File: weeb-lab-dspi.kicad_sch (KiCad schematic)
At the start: 11 parts, among them J1 SPDIF, J2 MONO RCA, U1 XIAO-RP2350-SMD

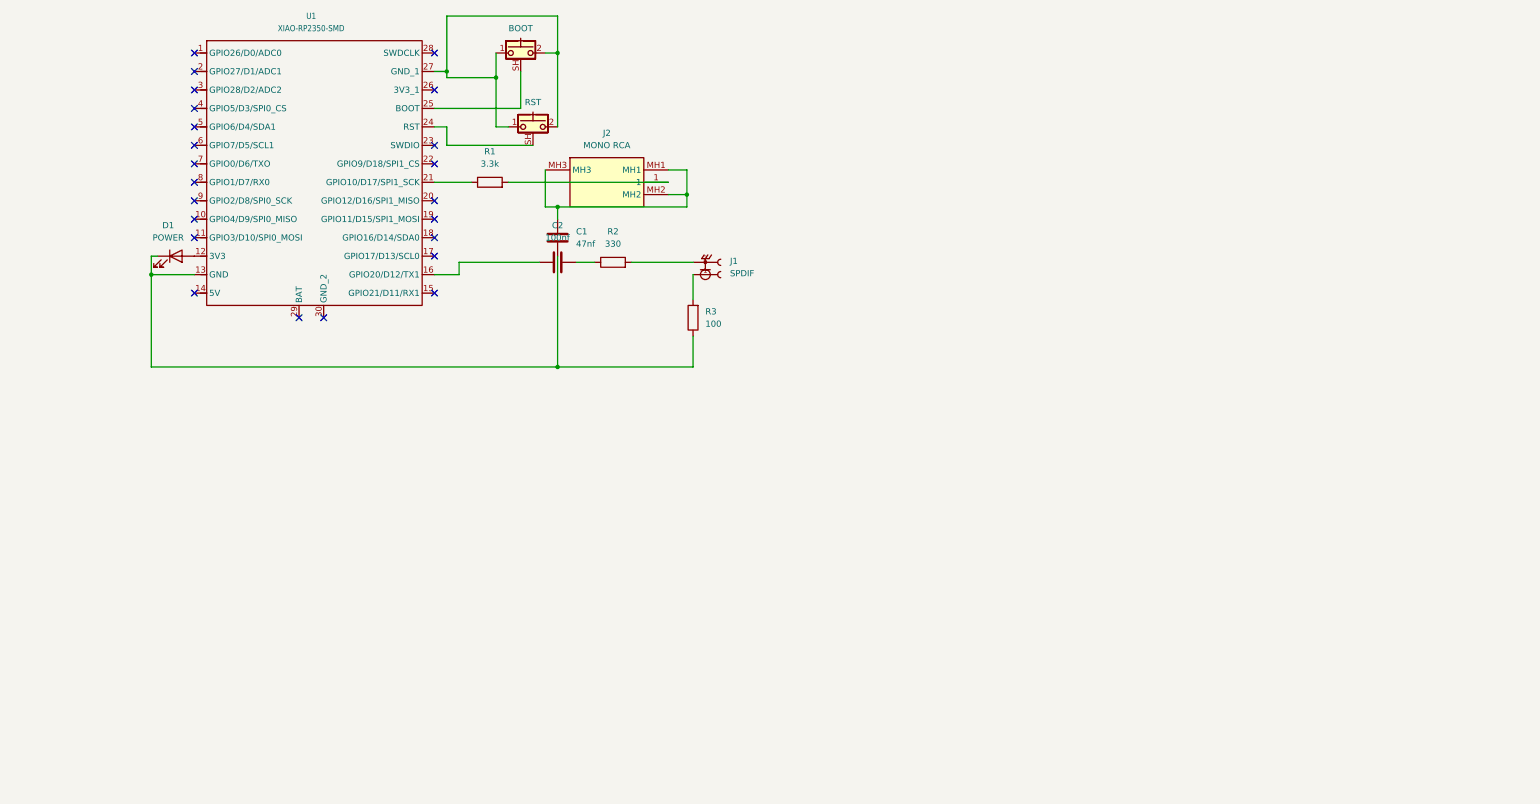
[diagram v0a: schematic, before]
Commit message: Routed PCB and added more parts
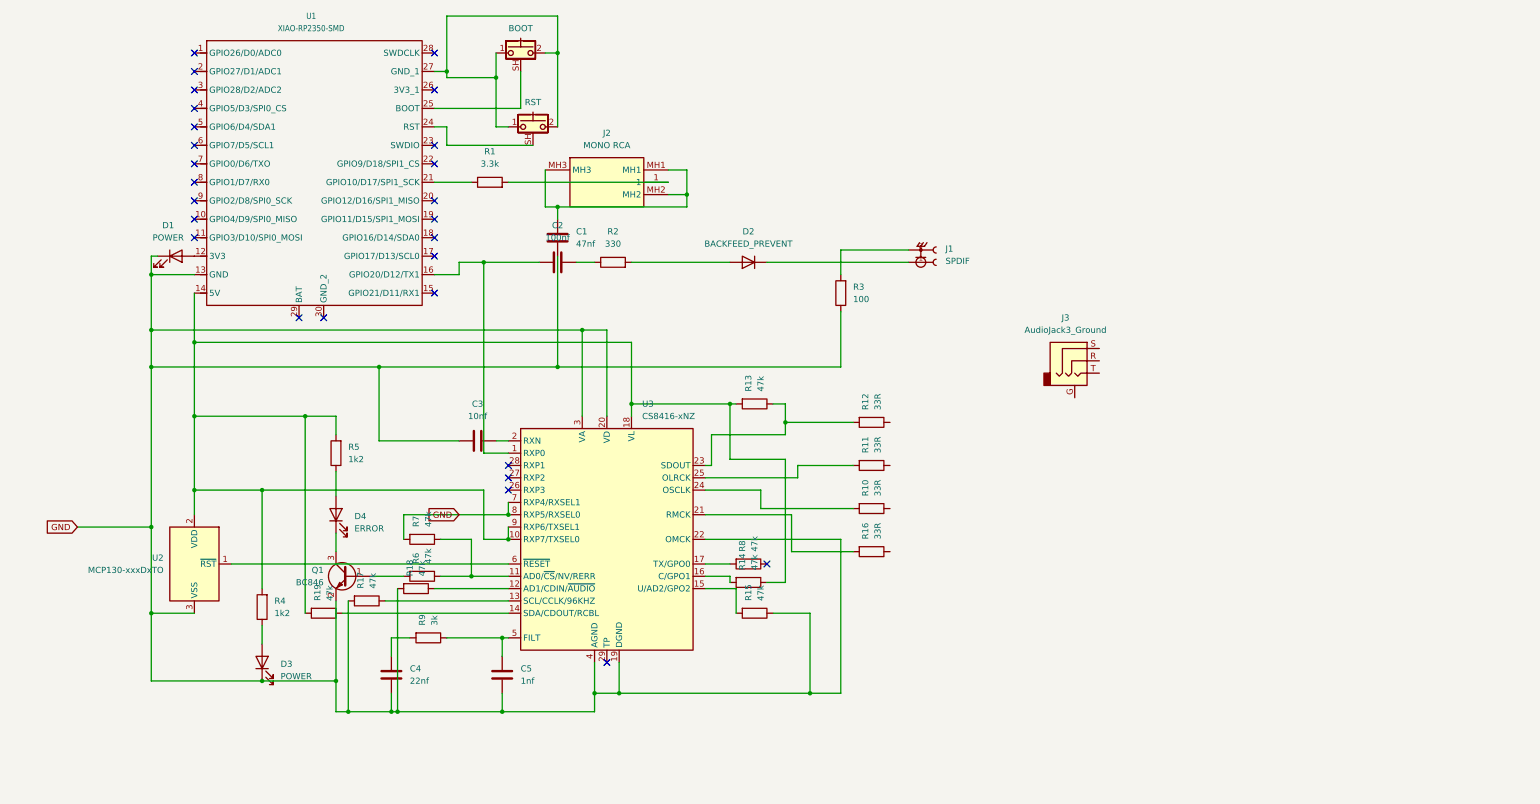
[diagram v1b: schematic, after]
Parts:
- added C3: 10nf, Capacitor_SMD:C_0402_1005Metric, symbol Device:C
- added C4: 22nf, Capacitor_SMD:C_0402_1005Metric, symbol Device:C
- added C5: 1nf, Capacitor_SMD:C_0402_1005Metric, symbol Device:C
- added D2: BACKFEED_PREVENT, Diode_SMD:D_0402_1005Metric, symbol Device:D
- added D3: POWER, LED_SMD:LED_0805_2012Metric, symbol Device:LED
- added D4: ERROR, LED_SMD:LED_0805_2012Metric, symbol Device:LED
- added J3: AudioJack3_Ground, Connector_Audio:Jack_3.5mm_KoreanHropartsElec_PJ-320D-4A_Horizontal, symbol Connector_Audio:AudioJack3_Ground
- added Q1: BC846, Package_TO_SOT_SMD:SOT-23-3, symbol Transistor_BJT:BC846
- added R10, R11, R12, R16: 33R, Resistor_SMD:R_0402_1005Metric, symbol Device:R
- added R13, R14, R15, R17, R18, R19, R6, R7, R8: 47k, Resistor_SMD:R_0402_1005Metric, symbol Device:R
- added R4, R5: 1k2, Resistor_SMD:R_0402_1005Metric, symbol Device:R
- added R9: 3k, Resistor_SMD:R_0402_1005Metric, symbol Device:R
- added U2: MCP130-xxxDxTO, Package_TO_SOT_THT:TO-92L_Inline_Wide, symbol Power_Supervisor:MCP130-xxxDxTO
- added U3: CS8416-xNZ, Package_SO:TSSOP-28_4.4x9.7mm_P0.65mm, symbol Audio:CS8416-xNZ
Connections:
- net GND: now reaches C1.2, D1.1 (K), R3.1, U1.13 (GND)
- net GND: now also C3.1, C4.2, C5.2, D3.1 (K), Q1.2 (E), R15.1, R17.2, R18.2, R7.2, U2.3 (VSS), U3.19 (DGND), U3.20 (VD), U3.22 (OMCK), U3.3 (VA), U3.4 (AGND), U3.7 (RXP4/RXSEL1), U3.8 (RXP5/RXSEL0)
- net at J1.2, J1.3, J1.4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: now also R3.2; no longer R2.2
- net at J1.1: now also D2.1 (K); no longer R3.2
- net at U1.14 (5V): now also R13.2, R14.1, R19.2, R4.2, R5.2, U2.2 (VDD), U3.10 (RXP7/TXSEL0), U3.18 (VL), U3.9 (RXP6/TXSEL1)
- net at C2.1, U1.16 (GPIO20/D12/TX1): now also U3.1 (RXP0)
- new net: R12.2, R13.1, U3.23 (SDOUT)
- new net: R17.1, U3.13 (SCL/CCLK/96KHZ)
- new net: D4.2 (A), R5.1
- new net: C4.1, R9.2
- new net: R10.2, U3.24 (OSCLK)
- new net: R11.2, U3.25 (OLRCK)
- new net: D2.2 (A), R2.2
- new net: R6.1, R7.1, U3.11 (AD0/~{CS}/NV/RERR)
- new net: R16.2, U3.21 (RMCK)
- new net: C3.2, U3.2 (RXN)
- new net: R14.2, U3.16 (C/GPO1)
- new net: Q1.1 (B), R6.2
- new net: U2.1 (~{RST}), U3.6 (~{RESET})
- new net: R19.1, U3.14 (SDA/CDOUT/RCBL)
- new net: R18.1, U3.12 (AD1/CDIN/~{AUDIO})
- new net: R15.2, U3.15 (U/AD2/GPO2)
- new net: R8.2, U3.17 (TX/GPO0)
- new net: C5.1, R9.1, U3.5 (FILT)
- new net: D4.1 (K), Q1.3 (C)
- new net: D3.2 (A), R4.1
- no-connect marks 23 -> 27
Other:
- moved on the sheet: J1, R3

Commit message: Almost  Complete
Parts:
- removed J3: AudioJack3_Ground, Connector_Audio:Jack_3.5mm_KoreanHropartsElec_PJ-320D-4A_Horizontal, symbol Connector_Audio:AudioJack3_Ground
- added C10, C11: 0.1uf, Capacitor_SMD:C_0402_1005Metric, symbol Device:C
- added C12, C13, C6, C7, C8, C9: 10uf, Capacitor_SMD:C_0402_1005Metric, symbol Device:C
- added D5: BACKFEED_PREVENT, Diode_SMD:D_0402_1005Metric, symbol Device:D
- added J4: AudioJack3_Ground, Connector_Audio:Jack_3.5mm_CUI_SJ-3524-SMT_Horizontal, symbol Connector_Audio:AudioJack3_Ground
- added LEFT1, RIGHT1: TPA6203A1DRB, Package_DFN_QFN:Texas_DRB0008A, symbol Amplifier_Audio:TPA6203A1DRB
- added U4: CS434x-xZZ, Package_SO:TSSOP-10_3x3mm_P0.5mm, symbol Analog_DAC:CS434x-xZZ
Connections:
- net GND: now also C10.2, C11.2, C6.2, C7.2, J4.G, J4.S, LEFT1.1 (~{SHUTDOWN}), LEFT1.4 (IN-), LEFT1.6 (V_{DD}), LEFT1.7 (GND), LEFT1.8 (V_{O-}), LEFT1.9 (GND), RIGHT1.1 (~{SHUTDOWN}), RIGHT1.4 (IN-), RIGHT1.6 (V_{DD}), RIGHT1.7 (GND), RIGHT1.8 (V_{O-}), RIGHT1.9 (GND), U4.8 (AGND), U4.9 (VA)
- net at R12.1: now also U4.1 (SDIN)
- net at R10.1: now also U4.2 (~{DEM}/SCLK)
- net at R11.1: now also U4.3 (LRCK)
- net at R16.1: now also U4.4 (MCLK)
- net at C2.1, U1.16 (GPIO20/D12/TX1): now also D5.2 (A); no longer U3.1 (RXP0)
- new net: C10.1, RIGHT1.2 (BYPASS)
- new net: C9.1, RIGHT1.3 (IN+)
- new net: C13.1, RIGHT1.5 (V_{O+})
- new net: C9.2, U4.10 (AOUTR)
- new net: C7.1, U4.5 (VQ)
- new net: C6.1, U4.6 (FILT+)
- new net: C8.2, U4.7 (AOUTL)
- new net: C13.2, J4.R
- new net: C12.2, J4.T
- new net: D5.1 (K), U3.1 (RXP0)
- new net: C12.1, LEFT1.5 (V_{O+})
- new net: C11.1, LEFT1.2 (BYPASS)
- new net: C8.1, LEFT1.3 (IN+)

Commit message: Finally
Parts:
- removed D1: POWER, LED_SMD:LED_0805_2012Metric, symbol Device:LED
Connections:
- net GND: no longer LEFT1.6 (V_{DD}), RIGHT1.6 (V_{DD}), U3.20 (VD), U3.3 (VA), U4.9 (VA)
- net at U1.12 (3V3): now also LEFT1.6 (V_{DD}), RIGHT1.6 (V_{DD}), U3.20 (VD), U3.3 (VA), U4.9 (VA)
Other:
- moved on the sheet: C1, C10, C11, C12, C13, C2, C3, C4, C5, C6, C7, C8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

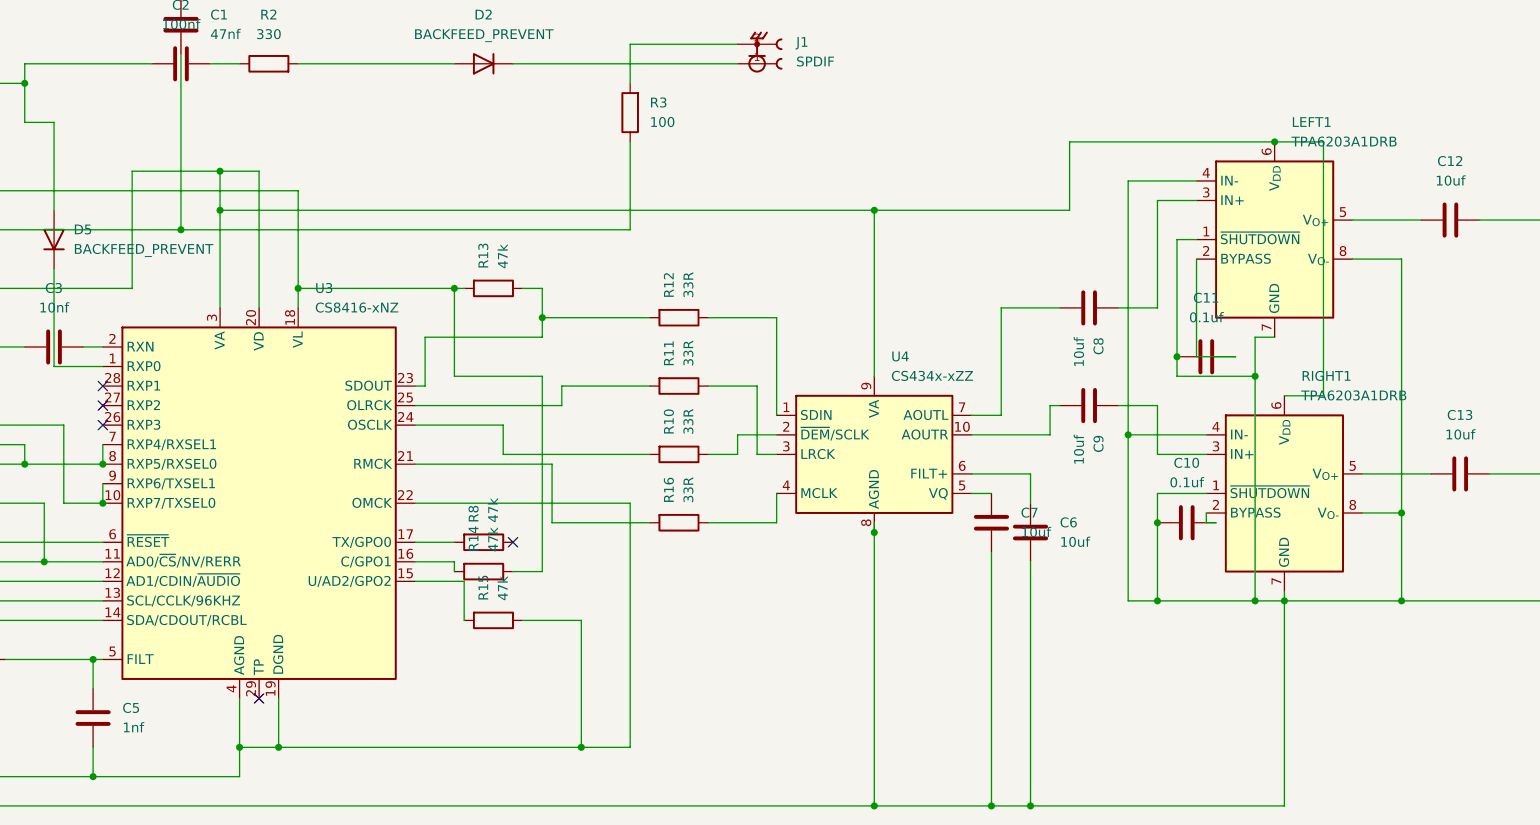
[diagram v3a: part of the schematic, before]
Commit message: Add power bypass caps
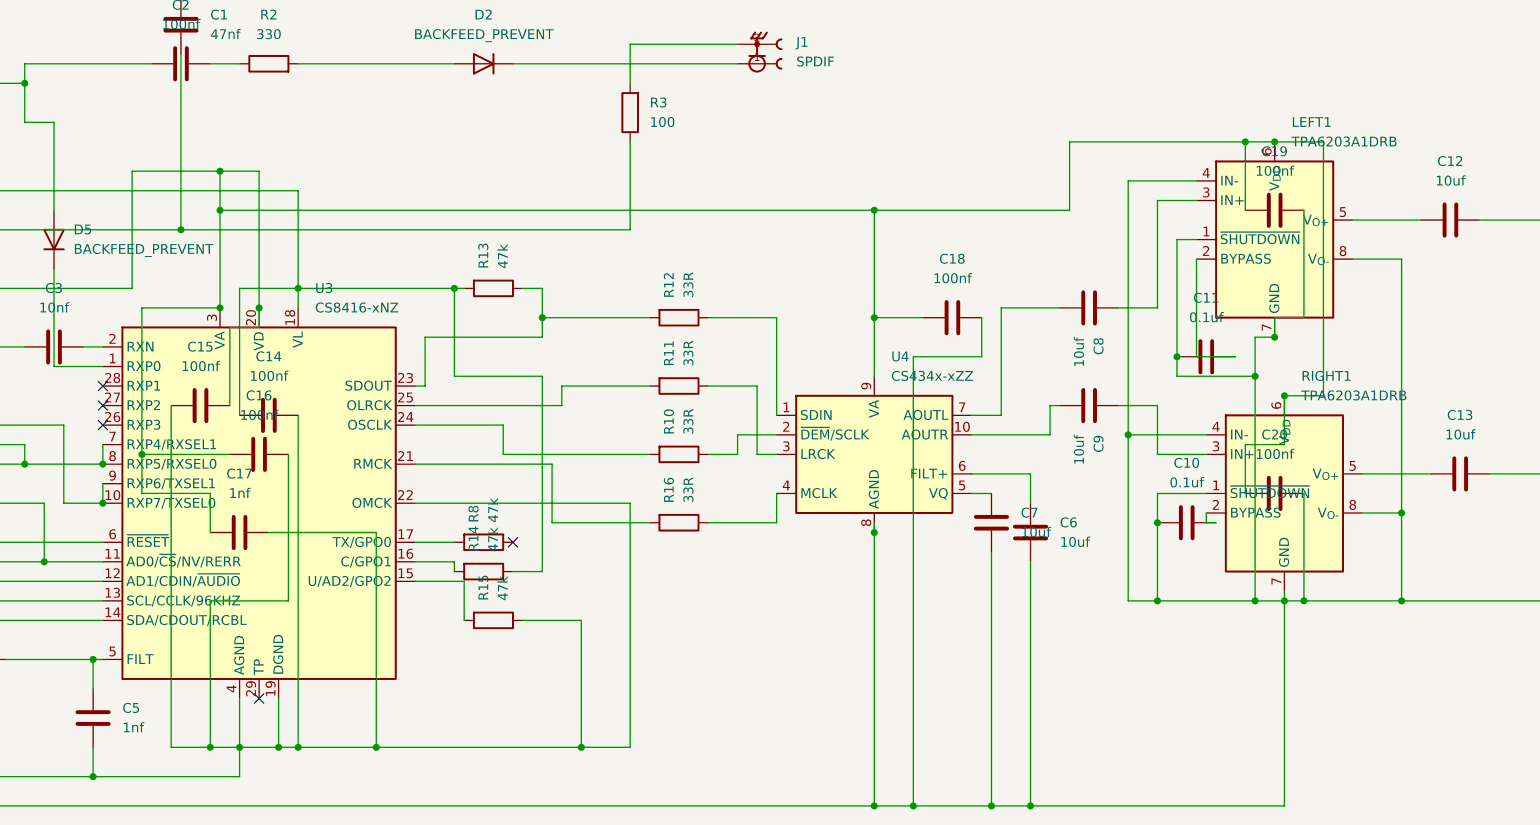
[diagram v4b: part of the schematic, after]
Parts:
- added C14, C15, C16, C18, C19, C20: 100nf, Capacitor_SMD:C_0402_1005Metric, symbol Device:C
- added C17: 1nf, Capacitor_SMD:C_0402_1005Metric, symbol Device:C
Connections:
- net GND: now also C14.2, C15.1, C16.2, C17.2, C18.2, C19.2, C20.2
- net at R13.2, R14.1, R19.2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: now also C14.1
- net at LEFT1.6 (V_{DD}), RIGHT1.6 (V_{DD}), U1.12 (3V3)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: now also C15.2, C16.1, C17.1, C18.1, C19.1, C20.1

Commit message: Adding Labeling
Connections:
- net GND: now also J1.2, J1.3, J1.4, J1.5
- net at J2.MH1, J2.MH2, J2.MH3: no longer C1.1
- net at D2.1 (K), J1.1: now also R3.2
- net at J2.1, R1.2: now also C1.1
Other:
- moved on the sheet: C1, C2
